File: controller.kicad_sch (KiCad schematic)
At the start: 15 parts, among them J1 Conn_01x09_Pin, J3 Conn_01x09_Pin, J7 Conn_01x04_Pin, SW1 SW_MEC_5G, SW2 SW_MEC_5G, U1 ESP32-C3-WROOM-02, U5 OLED_SSD1306

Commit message: wip schematic
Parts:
- removed J3: Conn_01x09_Pin, Connector_PinHeader_2.54mm:PinHeader_1x09_P2.54mm_Vertical, symbol Connector:Conn_01x09_Pin
- added R22, R23: 10k, Resistor_SMD:R_0603_1608Metric, symbol _PS_LIB:R_0603
- D6: value LED -> LED Blau
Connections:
- net GPIO20 is gone; now on net I2C_SDA: U1.11 (IO20/RXD)
- net GPIO21 is gone; now on net I2C_SCL: U1.12 (IO21/TXD)
- net +3.3V: now also R22.2, R23.2
- net GPIO0: now also J1.4 (Pin_4)
- net GPIO10: now also J1.5 (Pin_5)
- net GPIO8: no longer J1.5 (Pin_5)
- net I2C_SCL: now also R23.1
- net I2C_SDA: now also R22.1
- net PT100_1: now also U1.3 (IO4)
- net PT100_2: now also U1.4 (IO5)
- net SHDN1: now also U1.5 (IO6)
- net SHDN2: now also U1.6 (IO7)
- net GPIO1 renamed CHARGING
- net GPIO2 renamed READY
- net GPIO3 renamed UBAT
- net GPIO4: no longer names the net of J1.1 (Pin_1)
- net GPIO4: no longer U1.3 (IO4)
- net GPIO5: no longer names the net of J1.2 (Pin_2)
- net GPIO5: no longer U1.4 (IO5)
- net GPIO6: no longer names the net of J1.3 (Pin_3)
- net GPIO6: no longer U1.5 (IO6)
- removed net GPIO7: J1.4 (Pin_4), U1.6 (IO7)

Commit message: wip - schematic and layout
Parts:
- removed J1: Conn_01x09_Pin, Connector_PinHeader_2.54mm:PinHeader_1x09_P2.54mm_Vertical, symbol Connector:Conn_01x09_Pin
- removed J7: Conn_01x04_Pin, Connector_PinHeader_2.54mm:PinHeader_1x04_P2.54mm_Vertical, symbol Connector:Conn_01x04_Pin
- added C15, C16: 100n, Capacitor_SMD:C_0603_1608Metric, symbol _PS_LIB:C_0603
- added TP1, TP2, TP3, TP4, TP5: TestPoint, TestPoint:TestPoint_Pad_D1.5mm, symbol Connector:TestPoint
- added U8: BMP388, BMP388:PQFN50P200X200X80-10N, symbol BMP388:BMP388
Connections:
- net +3.3V: now also C15.1, C16.1, TP4.1, U8.1 (VDDIO), U8.10 (VDD), U8.6 (CSB); no longer R6.2
- net +5V: now also TP5.1
- net GND: now also C15.2, C16.2, TP3.1, U8.3 (VSS), U8.5 (SDO), U8.8 (VSS__1), U8.9 (VSS__2)
- net GPIO0: now also TP1.1
- net GPIO10: now also TP2.1
- net GPIO8: now also R6.2; no longer D6.2 (A), R6.1
- net I2C_SCL: now also R22.1, U1.11 (IO20/RXD), U8.2 (SCK); no longer R23.1, U1.12 (IO21/TXD)
- net I2C_SDA: now also R23.1, U1.12 (IO21/TXD), U8.4 (SDI); no longer R22.1, U1.11 (IO20/RXD)
- net PT100_1: now also U1.4 (IO5); no longer U1.3 (IO4)
- net PT100_2: now also U1.3 (IO4); no longer U1.4 (IO5)
- new net: D6.2 (A), R6.1
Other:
- note added: "BMP388 Address: 1110110 x76"
- moved on the sheet: R6

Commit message: wip
lcsc part numbers
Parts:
- C4: value 10u 25V -> 10u 10V; LCSC (none) -> C2959727
- D6: LCSC (none) -> C965807
- R22, R23, R4, R5: LCSC (none) -> C25804
- R6: LCSC (none) -> C431786
- SW1, SW2: LCSC (none) -> C720477
- U1: LCSC (none) -> C2934560
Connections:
- net CHARGING: now also U1.10 (IO10); no longer U1.17 (IO1)
- net PT100_1: now also U1.17 (IO1); no longer U1.4 (IO5)
- net PT100_2: now also U1.16 (IO2); no longer U1.3 (IO4)
- net READY: now also U1.18 (IO0); no longer U1.16 (IO2)
- net GPIO0: no longer names the net of TP1.1
- net GPIO0: now also U1.3 (IO4); no longer U1.18 (IO0)
- net GPIO10: no longer names the net of TP2.1
- net GPIO10: now also U1.4 (IO5); no longer U1.10 (IO10)
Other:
- moved on the sheet: TP1, TP2
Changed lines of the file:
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@@
 	(wire
 		(pts
-			(xy 186.69 95.25) (xy 203.2 95.25)
+			(xy 199.39 95.25) (xy 203.2 95.25)
 		)
 		(stroke
@@
 	(wire
 		(pts
-			(xy 186.69 69.85) (xy 203.2 69.85)
+			(xy 199.39 69.85) (xy 203.2 69.85)
 		)
 		(stroke
@@
 		)
 	)
-	(label "GPIO10"
-		(at 186.69 95.25 0)
-		(effects
-			(font
-				(size 1.27 1.27)
-			)
-			(justify left bottom)
-		)
-	)
 	(label "I2C_SDA"
 		(at 242.57 67.31 0)
@@
 		)
 	)
-	(label "GPIO0"
-		(at 186.69 69.85 0)
-		(effects
-			(font
-				(size 1.27 1.27)
-			)
-			(justify left bottom)
-		)
-	)
 	(hierarchical_label "PT100_1"
 		(shape input)
-		(at 199.39 82.55 180)
+		(at 199.39 72.39 180)
 		(effects
 			(font
@@
 	(hierarchical_label "PT100_2"
 		(shape input)
-		(at 199.39 80.01 180)
+		(at 199.39 74.93 180)
 		(effects
 			(font
@@
 	(hierarchical_label "READY"
 		(shape input)
-		(at 199.39 74.93 180)
+		(at 199.39 69.85 180)
 		(effects
 			(font
@@
 	(hierarchical_label "CHARGING"
 		(shape input)
-		(at 199.39 72.39 180)
+		(at 199.39 95.25 180)
 		(effects
 			(font
@@
 	(symbol
 		(lib_id "Connector:TestPoint")
-		(at 186.69 69.85 90)
+		(at 199.39 80.01 90)
 		(unit 1)
 		(exclude_from_sim no)
@@
 		(fields_autoplaced yes)
 		(property "Reference" "TP1"
-			(at 183.388 67.31 90)
+			(at 194.31 80.0099 90)
 			(effects
 				(font
 					(size 1.27 1.27)
 				)
+				(justify left)
 			)
 		)
 		(property "Value" "TestPoint"
-			(at 183.388 74.93 90)
+			(at 196.088 85.09 90)
 			(effects
 				(font
@@
 		)
 		(property "Footprint" "TestPoint:TestPoint_Pad_D1.5mm"
-			(at 186.69 64.77 0)
+			(at 199.39 74.93 0)
 			(effects
 				(font
@@
 		)
 		(property "Datasheet" "~"
-			(at 186.69 64.77 0)
+			(at 199.39 74.93 0)
 			(effects
 				(font
@@
 		)
 		(property "Description" "test point"
-			(at 186.69 69.85 0)
+			(at 199.39 80.01 0)
 			(effects
 				(font
@@
 		)
 		(property "Characteristics" ""
-			(at 186.69 69.85 0)
+			(at 199.39 80.01 0)
 			(effects
 				(font
@@
 		)
 		(property "LCSC" ""
-			(at 186.69 69.85 0)
+			(at 199.39 80.01 0)
 			(effects
 				(font
@@
 			)
 		)
+		(property "Characteristics" ""
+			(at 158.75 92.71 0)
+			(effects
+				(font
+					(size 1.27 1.27)
+				)
+				(hide yes)
+			)
+		)
+		(property "LCSC" "C720477"
+			(at 158.75 92.71 0)
+			(effects
+				(font
+					(size 1.27 1.27)
+				)
+				(hide yes)
+			)
+		)
 		(pin "1"
 		)
@@
 			)
 		)
+		(property "Characteristics" ""
+			(at 264.16 58.42 0)
+			(effects
+				(font
+					(size 1.27 1.27)
+				)
+				(hide yes)
+			)
+		)
+		(property "LCSC" "C25804"
+			(at 264.16 58.42 0)
+			(effects
+				(font
+					(size 1.27 1.27)
+				)
+				(hide yes)
+			)
+		)
 		(pin "1"
 		)
@@
 			)
 		)
+		(property "Characteristics" ""
+			(at 198.12 57.15 0)
+			(effects
+				(font
+					(size 1.27 1.27)
+				)
+				(hide yes)
+			)
+		)
+		(property "LCSC" "C25804"
+			(at 198.12 57.15 0)
+			(effects
+				(font
+					(size 1.27 1.27)
+				)
+				(hide yes)
+			)
+		)
 		(pin "1"
 		)
@@
 			)
 		)
+		(property "Characteristics" ""
+			(at 170.18 64.77 0)
+			(effects
+				(font
+					(size 1.27 1.27)
+				)
+				(hide yes)
+			)
+		)
+		(property "LCSC" "C720477"
+			(at 170.18 64.77 0)
+			(effects
+				(font
+					(size 1.27 1.27)
+				)
+				(hide yes)
+			)
+		)
 		(pin "1"
 		)
@@
 			)
 		)
+		(property "Characteristics" ""
+			(at 182.88 90.17 0)
+			(effects
+				(font
+					(size 1.27 1.27)
+				)
+				(hide yes)
+			)
+		)
+		(property "LCSC" "C25804"
+			(at 182.88 90.17 0)
+			(effects
+				(font
+					(size 1.27 1.27)
+				)
+				(hide yes)
+			)
+		)
 		(pin "1"
 		)
@@
 	(symbol
 		(lib_id "Connector:TestPoint")
-		(at 186.69 95.25 90)
+		(at 199.39 82.55 90)
 		(unit 1)
 		(exclude_from_sim no)
@@
 		(fields_autoplaced yes)
 		(property "Reference" "TP2"
-			(at 181.61 95.2499 90)
+			(at 194.31 82.5499 90)
 			(effects
 				(font
@@
 		)
 		(property "Value" "TestPoint"
-			(at 183.388 100.33 90)
+			(at 196.088 87.63 90)
 			(effects
 				(font
@@
 		)
 		(property "Footprint" "TestPoint:TestPoint_Pad_D1.5mm"
-			(at 186.69 90.17 0)
+			(at 199.39 77.47 0)
 			(effects
 				(font
@@
 		)
 		(property "Datasheet" "~"
-			(at 186.69 90.17 0)
+			(at 199.39 77.47 0)
 			(effects
 				(font
@@
 		)
 		(property "Description" "test point"
-			(at 186.69 95.25 0)
+			(at 199.39 82.55 0)
 			(effects
 				(font
@@
 		)
 		(property "Characteristics" ""
-			(at 186.69 95.25 0)
+			(at 199.39 82.55 0)
 			(effects
 				(font
@@
 		)
 		(property "LCSC" ""
-			(at 186.69 95.25 0)
+			(at 199.39 82.55 0)
 			(effects
 				(font
@@
 			)
 		)
+		(property "Characteristics" ""
+			(at 135.89 88.9 0)
+			(effects
+				(font
+					(size 1.27 1.27)
+				)
+				(hide yes)
+			)
+		)
+		(property "LCSC" "C431786"
+			(at 135.89 88.9 0)
+			(effects
+				(font
+					(size 1.27 1.27)
+				)
+				(hide yes)
+			)
+		)
 		(pin "1"
 		)
@@
 			)
 		)
-		(property "LCSC" ""
+		(property "LCSC" "C965807"
 			(at 135.89 97.79 0)
 			(effects
@@
 			)
 		)
+		(property "Characteristics" ""
+			(at 254 58.42 0)
+			(effects
+				(font
+					(size 1.27 1.27)
+				)
+				(hide yes)
+			)
+		)
+		(property "LCSC" "C25804"
+			(at 254 58.42 0)
+			(effects
+				(font
+					(size 1.27 1.27)
+				)
+				(hide yes)
+			)
+		)
 		(pin "1"
 		)
@@
 			)
 		)
-		(property "LCSC" ""
+		(property "LCSC" "C2934560"
 			(at 218.44 82.55 0)
 			(effects
@@
 			)
 		)
-		(property "Value" "10u 25V"
+		(property "Value" "10u 10V"
 			(at 227.33 48.2599 0)
 			(effects
@@
 			(at 223.52 46.99 0)
 			(effects
+				(font
+					(size 1.27 1.27)
+				)
+				(hide yes)
+			)
+		)
+		(property "Characteristics" ""
+			(at 223.52 46.99 0)
+			(effects
+				(font
+					(size 1.27 1.27)
+				)
+				(hide yes)
+			)
+		)
+		(property "LCSC" "C2959727"
+			(at 223.52 46.99 0)
+			(effects

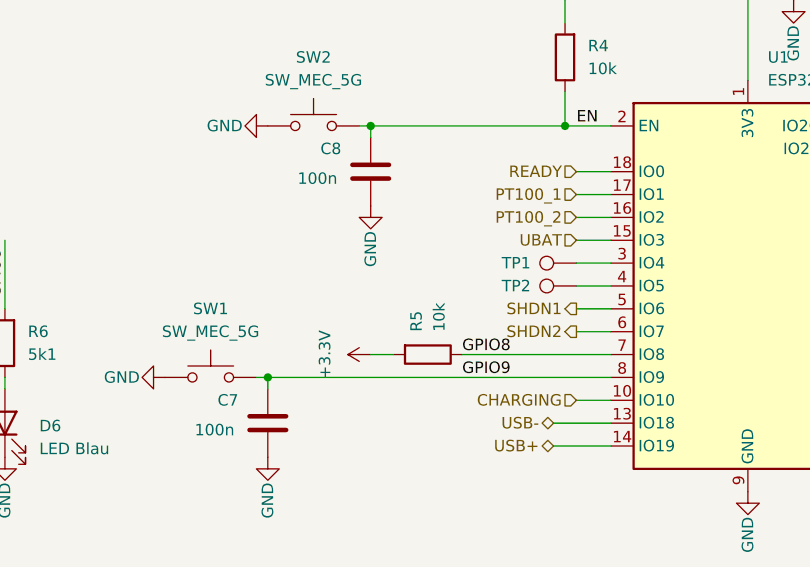
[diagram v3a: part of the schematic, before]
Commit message: level shift for op en added
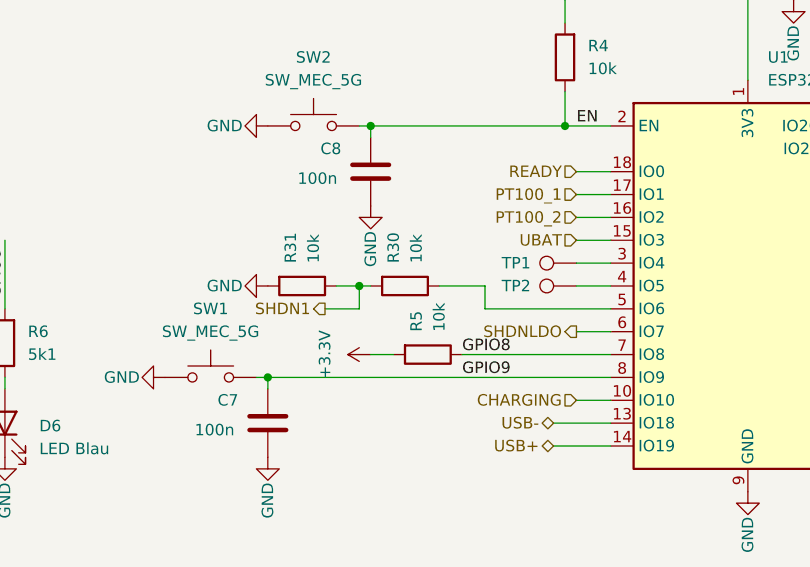
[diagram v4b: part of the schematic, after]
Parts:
- added R30, R31: 10k, Resistor_SMD:R_0603_1608Metric, symbol _PS_LIB:R_0603
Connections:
- net GND: now also R31.2
- net SHDN1: now also R30.2, R31.1; no longer U1.5 (IO6)
- net SHDN2 renamed SHDNLDO
- new net: R30.1, U1.5 (IO6)
